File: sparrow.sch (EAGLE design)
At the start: 40 parts, among them Y1 12MHz

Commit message: Further work
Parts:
- added ADC: HEADER-1X8ROUND, anykey:HEADER-1X8ROUND
- added C22, C23: 18p, anykey:CAP_CERAMIC0603
- added C24, C25, C26, C30, C31, C32, C33: 100n, anykey:CAP_CERAMIC0603
- added C27: 1µ, anykey:CAP_CERAMIC0603
- added C28: 470p, anykey:CAP_CERAMIC0603
- added C29: 10µ, anykey:CAP_CERAMIC0603
- added FERRITE_BEAD: BLM18PG121SN1D, anykey:INDUCTOR0603
- added IC1: LAN8720AQFN, anykey:LAN8720AQFN
- added LED2, LED3: (no value), anykey:LED0603
- added P2: ETHERNET_JACKPULSEJACK, anykey:ETHERNET_JACKPULSEJACK
- added R10, R11, R12, R13: 12K, anykey:R-EU_0603
- added R14, R15: 330, anykey:R-EU_0603
- added R16: 12K1, anykey:R-EU_0603
- added R17, R18, R19, R20: 49R9, anykey:R-EU_0603
- added X1: ABS07-32768, anykey:CRYSTAL1206
- added Y2: (no value), anykey:CRYSTAL_WITH_GROUND25X20
- P1: value HEADER-2X5SMD-1.27MM -> DEBUG
- renumbered U$18 to P1
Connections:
- new net ADC0: ADC.1, MCU.ADC0_0
- new net ADC1: ADC.2, MCU.ADC0_1
- new net ADC2: ADC.3, MCU.ADC0_2
- new net ADC3: ADC.4, MCU.ADC0_3
- new net ADC4: ADC.5, MCU.ADC0_4
- new net ADC5: ADC.6, MCU.ADC0_5
- new net ADC6: ADC.7, MCU.ADC0_6
- new net ADC7: ADC.8, MCU.ADC0_7
- new net ETH_!RST: IC1.!RST
- new net ETH_CRS_DV: IC1.CRS_DV/MODE2, MCU.P1_16
- new net ETH_MDC: IC1.MDC, MCU.P7_7
- new net ETH_MDIO: IC1.MDIO, MCU.P1_17
- new net ETH_RBIAS: IC1.RBIAS, R16.2
- new net ETH_REFCLK: IC1.!INT!/REFCLK0
- new net ETH_RTERM: C33.P$1, R19.2, R20.1
- new net ETH_RXD0: IC1.RXD0/MODE0, MCU.P1_15
- new net ETH_RXD1: IC1.RXD1/MODE1, MCU.P0_0
- new net ETH_RXER: IC1.RXER/PHYAD0
- new net ETH_RXN: IC1.RXN, P2.RD-, R20.2
- new net ETH_RXP: IC1.RXP, P2.RD+, R19.1
- new net ETH_TTERM: C32.P$1, R17.2, R18.1
- new net ETH_TXD0: IC1.TXD0, MCU.P1_18
- new net ETH_TXD1: IC1.TXD1, MCU.P1_20
- new net ETH_TXEN: IC1.TXEN, MCU.P0_1
- new net ETH_TXN: IC1.TXN, P2.TD-, R18.2
- new net ETH_TXP: IC1.TXP, P2.TD+, R17.1
- new net ETH_VDDCR: C27.P$1, C28.P$1, IC1.VDDCR
- new net ETH_XTAL1: IC1.XTAL1/CLKIN, Y2.2
- new net ETH_XTAL2: IC1.XTAL2, Y2.1
- new net N$10: IC1.LED2/!INTSEL, LED3.ANODE
- new net N$11: IC1.LED1/REGOFF, LED2.ANODE
- new net N$3: C22.P$1, MCU.RTCX1, X1.2
- new net N$4: C23.P$1, MCU.RTCX2, X1.1
- new net N$6: LED2.CATHODE, R14.2
- new net N$7: LED3.CATHODE, R15.2
- new net SWDCLK: MCU.TCK_SWDCLK, P1.4, R13.2
- new net SWDIO: MCU.TMS_SWDIO, P1.2, R10.1
- new net TDI: MCU.TDI, P1.8, R12.1
- new net TDO_SWO: MCU.TDO_SWO, P1.6, R11.1
- new net VETH33: C24.P$1, C25.P$1, C30.P$1, C31.P$1, FERRITE_BEAD.2, IC1.VDD1A, IC1.VDD2A, P2.RC, P2.TC
- net !RESET: now also P1.10
- net GND: now also C22.P$2, C23.P$2, C24.P$2, C25.P$2, C26.P$2, C27.P$2, C28.P$2, C29.P$2, C30.P$2, C31.P$2, C32.P$2, C33.P$2, IC1.VSS, P1.3, P1.5, P1.9, P2.GND, R13.1, R14.1, R15.1, R16.1, Y2.GND
- net VD33: now also C26.P$1, C29.P$1, FERRITE_BEAD.1, IC1.VDDIO, P1.1, R10.2, R11.2, R12.2

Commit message: Further work
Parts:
- removed C30: 100n, anykey:CAP_CERAMIC0603
- removed FERRITE_BEAD: BLM18PG121SN1D, anykey:INDUCTOR0603
- removed LED2, LED3: (no value), anykey:LED0603
- removed P2: ETHERNET_JACKPULSEJACK, anykey:ETHERNET_JACKPULSEJACK
- added ANT1, ANT2: (no value), anykey:ANTENNA_MONOPOLE1206
- added C34, C52, C53, C54: (no value), anykey:CAP_CERAMIC0603
- added C35, C36, C37, C56: 1µ, anykey:CAP_CERAMIC0603
- added C38, C39, C43, C45, C47, C49: 0.1µ, anykey:CAP_CERAMIC0603
- added C40, C41: 22µ, anykey:CAP_CERAMIC0603
- added C42, C44, C46, C48: 10µ, anykey:CAP_CERAMIC0603
- added C50, C51: 47µ, anykey:CAP_CERAMIC0805
- added C55: (no value), anykey:CAP_CERAMIC0402
- added C57, C59: 22µ 10V, anykey:CAP_CERAMIC0805
- added C58: 100n, anykey:CAP_CERAMIC0603
- added C60: 150µ 10V, anykey:CPOL-EU1210
- added C61: 47n, anykey:CAP_CERAMIC0402
- added C62, C63, C64: 100n, anykey:CAP_CERAMIC0402
- added C65: 1n, anykey:CAP_CERAMIC0402
- added C66, C67: 12p, anykey:CAP_CERAMIC0402
- added C68, C69: 9p, anykey:CAP_CERAMIC0402
- added C70, C72: 2.2p, anykey:CAP_CERAMIC0402
- added C71, C73: 1p, anykey:CAP_CERAMIC0402
- added D1, D2, D3, D4, D5: (no value), anykey:DIODESOD123FL
- added HEADPHONE, LINEIN: (no value), anykey:HEADER-1X3ROUND
- added IC2: TLV320AIC3100VIAS, anykey:TLV320AIC3100VIAS
- added IC3: TPS2500, anykey:TPS2500SON10
- added JP1, U$44, U$45, U$50, U$51, U$52, U$53, U$54, U$55, U$56, U$61, U$62: JUMPERSOLDER_CLOSED, anykey:JUMPERSOLDER_CLOSED
- added L10: 3.3nH, anykey:INDUCTOR0402
- added L2, L3, L4: BLM18PG121SN1D, anykey:INDUCTOR0603
- added L5, L6: (no value), anykey:INDUCTOR0402
- added L7: 2.2µ, anykey:INDUCTOR40X40MM
- added L8: 4.7nH, anykey:INDUCTOR0402
- added L9: 10nH, anykey:INDUCTOR0402
- added MCU1: NRF51822QFN48, anykey:NRF51822QFN48
- added MIC, SPEAKER: (no value), anykey:HEADER-1X2ROUND
- added P3: HEADER-1X9ROUND, anykey:HEADER-1X9ROUND
- added P4: SD_CARD, anykey:SD_CARD
- added P5, P6: (no value), anykey:HEADER-1X5ROUND
- added R21, R29, R34: (no value), anykey:R-EU_0603
- added R22, R23: 2K2, anykey:R-EU_0603
- added R24, R25, R27, R28, R31, R33, R35, R36: 100K, anykey:R-EU_0603
- added R26: 40K2, anykey:R-EU_0603
- added R30, R32: 10K, anykey:R-EU_0603
- added T1, T2, T3: (no value), anykey:PMOS_ENH
- added U$6: ETHERNET_JACK_LEDSRB1-125BAG1A, anykey:ETHERNET_JACK_LEDSRB1-125BAG1A
- added U$68: HEADER-2X5SMD-1.27MM, anykey:HEADER-2X5SMD-1.27MM
- added WIFI1: CC3000EXTENDED, anykey:CC3000EXTENDED
- added X2: 50MHZ, anykey:OSCILLATOR25X20
- added X3: 32.768KHz, anykey:CRYSTAL1206
- L1: value 10u -> 10µH
- Y2: value (none) -> 16MHz
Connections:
- net ETH_RXER renamed ETH_RX_ER
- removed net ETH_REFCLK: IC1.!INT!/REFCLK0
- removed net ETH_XTAL1: IC1.XTAL1/CLKIN, Y2.2
- removed net ETH_XTAL2: IC1.XTAL2, Y2.1
- removed net N$10: IC1.LED2/!INTSEL, LED3.ANODE
- removed net VEXT: MCU.USB0_VBUS, USB0.VBUS
- removed net VUSB: C9.P$1, PWR1.EN_BUCK, PWR1.VCC, R4.2
- new net !AUDIO_PWR: T3.G
- new net !ETH_PWR: T1.G
- new net !WIFI_PWR: T2.G
- new net 5V_BOOST_SW: IC3.SW, L7.2
- new net 5V_GEN_EN: IC3.EN, R29.2
- new net 5V_ILIM: IC3.ILIM, R26.2
- new net AUDIO_!RESET: IC2.!RESET
- new net AUDIO_BCLK: IC2.BCLK, U$54.P$2, U$55.P$2
- new net AUDIO_DIN: IC2.DIN, U$50.P$2
- new net AUDIO_DOUT: IC2.DOUT, U$51.P$2
- new net AUDIO_GPIO1: IC2.GPIO1
- new net AUDIO_MCLK: IC2.MCLK, U$56.P$2
- new net AUDIO_SCL: IC2.SCL, U$62.P$2
- new net AUDIO_SDA: IC2.SDA, U$61.P$2
- new net AUDIO_WCLK: IC2.WCLK, U$52.P$2, U$53.P$2
- new net ETH_LED1: IC1.LED1/REGOFF, R14.2
- new net ETH_LED2: IC1.LED2/!INTSEL, R15.2
- new net ETH_REF_CLK: IC1.XTAL1/CLKIN, MCU.CLK0, X2.CLK
- new net HPL: C50.P$1, IC2.HPL
- new net HPR: C51.P$1, IC2.HPR
- new net HP_L: C50.P$2, HEADPHONE.1
- new net HP_R: C51.P$2, HEADPHONE.3
- new net I2C0_IRQA: P5.4
- new net I2C0_IRQB: P6.4
- new net I2C0_SCL: MCU.I2C0_SCL, P5.2, P6.2, R22.1, U$62.P$1
- new net I2C0_SDA: MCU.I2C0_SDA, P5.3, P6.3, R23.1, U$61.P$1
- new net I2S_MCLK: MCU.P1_19, P3.3, U$56.P$1
- new net I2S_RX_SCK: MCU.P6_0, P3.4, U$55.P$1
- new net I2S_RX_SD: MCU.P6_2, P3.8, U$51.P$1
- new net I2S_RX_WS: MCU.P6_1, P3.6, U$53.P$1
- new net I2S_TX_SCK: MCU.P4_7, P3.5, U$54.P$1
- new net I2S_TX_SD: MCU.P7_2, P3.9, U$50.P$1
- new net I2S_TX_WS: MCU.P7_1, P3.7, U$52.P$1
- new net JP1: JP1.P$2, WIFI1.SCL_EEPROM
- new net LINEIN1: C52.P$1, LINEIN.3
- new net LINEIN2: C53.P$1, LINEIN.1
- new net MIC: C54.P$1, IC2.VOL/MICDET, MIC.2, R21.1
- new net MIC1LM: C52.P$2, IC2.MIC1LM
- new net MIC1LP: C53.P$2, IC2.MIC1LP
- new net MIC1RP: C54.P$2, IC2.MIC1RP
- new net MICBIAS: IC2.MICBIAS, R21.2
- new net N$12: U$45.P$1, WIFI1.SDA_CC3000
- new net N$13: C67.P$1, MCU1.XC2, Y2.1
- new net N$14: C66.P$1, MCU1.XC1, Y2.2
- new net N$15: C62.P$1, MCU1.DEC1
- new net N$16: C61.P$1, MCU1.DEC2
- new net N$17: C69.P$2, MCU1.P0.27, X3.1
- new net N$18: C68.P$2, MCU1.P0.26, X3.2
- new net N$19: R14.1, U$6.LED1A
- new net N$20: D5.ANODE, U$44.P$2
- new net N$21: L8.1, L9.2, MCU1.ANT1
- new net N$22: R15.1, U$6.LED2K
- new net N$23: C70.P$1, L8.2, MCU1.ANT2
- new net N$24: C70.P$2, C71.P$2, L10.1
- new net N$25: ANT2.ANT, C73.P$2, L10.2
- new net N$27: C72.P$2, L9.1, MCU1.VDD_PA
- new net N$5: C55.P$1, L5.2, WIFI1.RF_ANT
- new net NRF_SWDCLK: MCU1.SWDCLK, R34.2, U$68.4
- new net NRF_SWDIO: MCU1.SWDIO/NRESET, U$68.2
- new net SD_CD: MCU.P1_13, P4.CD, R24.1
- new net SD_CLK: MCU.CLK2, P4.5
- new net SD_CMD: MCU.P1_6, P4.2
- new net SD_DAT0: MCU.P1_9, P4.7
- new net SD_DAT1: MCU.P1_10, P4.8
- new net SD_DAT2: MCU.P1_11, P4.9
- new net SD_DAT3: MCU.P1_12, P4.1
- new net SD_WP: P4.WP, R25.1
- new net SPKM: IC2.SPKM, SPEAKER.2
- new net SPKP: IC2.SPKP, SPEAKER.1
- new net USB0_VBUS: MCU.USB0_VBUS, R30.1, R31.2
- new net USB1_VBUS: MCU.P2_5, R32.1, R33.2
- new net USB_PPWR: IC3.ENUSB, MCU.P2_0, R28.2
- new net USB_PWR_FAULT: IC3.!FAULT, MCU.P2_1, R27.1
- new net V5_GEN: C59.P$1, D3.ANODE, IC3.AUX
- new net V5_IN: C9.P$1, D1.CATHODE, D2.CATHODE, PWR1.EN_BUCK, PWR1.VCC, R35.2, R4.2
- new net V5_IN_SENSE: R35.1, R36.2
- new net V5_OUT: D3.CATHODE, D4.CATHODE, D5.CATHODE
- new net VAUDIO33: C37.P$1, C42.P$1, C43.P$1, C44.P$1, C45.P$1, C46.P$1, C47.P$1, C48.P$1, C49.P$1, IC2.AVDD, IC2.DVDD, IC2.HPVDD, IC2.IOVDD, L4.2
- new net VAUDIO5: C38.P$1, C39.P$1, C40.P$1, C41.P$1, IC2.SPKVDD
- new net VETH_RAW: L2.1, T1.D
- new net VETH_RAW1: L3.1, T2.D
- new net VETH_RAW2: L4.1, T3.D
- new net VPOWER: D1.ANODE, D4.ANODE
- new net VUSB0: C60.+, IC3.USB, R30.2, USB0.VBUS
- new net VUSB1: D2.ANODE, R32.2, U$44.P$1, USB1.VBUS
- new net VWIFI33: C36.P$1, L3.2, WIFI1.VBAT_IN, WIFI1.VIO_HOST
- new net WIFI_CLK: WIFI1.SPI_CLK
- new net WIFI_IRQ: WIFI1.SPI_IRQ
- new net WIFI_MISO: WIFI1.SPI_DOUT
- new net WIFI_MOSI: WIFI1.SPI_DIN
- new net WIFI_SSEL: WIFI1.SPI_CS
- new net WIFI_SW_EN: WIFI1.VBAT_SW_EN
- net ETH_RXN: now also U$6.RD-; no longer P2.RD-
- net ETH_RXP: now also U$6.RD+; no longer P2.RD+
- net ETH_TXN: now also U$6.TD-; no longer P2.TD-
- net ETH_TXP: now also U$6.TD+; no longer P2.TD+
- net GND: now also C34.P$2, C35.P$2, C36.P$2, C37.P$2, C38.P$2, C39.P$2, C40.P$2, C41.P$2, C42.P$2, C43.P$2, C44.P$2, C45.P$2, C46.P$2, C47.P$2, C48.P$2, C49.P$2, C56.P$2, C57.P$2, C58.P$2, C59.P$2, C60.-, C61.P$2, C62.P$2, C63.P$2, C64.P$2, C65.P$2, C66.P$2, C67.P$2, C68.P$1, C69.P$1, C71.P$1, C72.P$1, C73.P$1, HEADPHONE.2, IC2.AVSS, IC2.DVSS, IC2.HPVSS, IC2.IOVSS, IC2.SPKVSS, IC3.GND, IC3.PGND, L5.1, L6.1, LINEIN.2, MIC.1, P3.1, P4.3, P4.6, P4.GND, P5.5, P6.5, R26.1, R28.1, R29.1, R31.1, R33.1, R34.1, R36.1, U$6.GND, U$6.LED1K, U$68.3, U$68.5, U$68.7, U$68.9, WIFI1.GND, X2.GND; no longer C30.P$2, P2.GND, R14.1, R15.1
- net N$11: now also JP1.P$1, WIFI1.SCL_CC3000; no longer IC1.LED1/REGOFF, LED2.ANODE
- net N$6: now also ANT1.ANT, C55.P$2, L6.2; no longer LED2.CATHODE, R14.2
- net N$7: now also U$45.P$2, WIFI1.SDA_EEPROM; no longer LED3.CATHODE, R15.2
- net VBAT: now also C57.P$1, C58.P$1, IC3.IN, L7.1
- net VD33: now also C56.P$1, C63.P$1, C64.P$1, C65.P$1, MCU1.AVDD, MCU1.VDD, P3.2, P4.4, P5.1, P6.1, R22.2, R23.2, R24.2, R25.2, R27.2, T1.S, T2.S, T3.S, U$68.1; no longer C26.P$1, C29.P$1, FERRITE_BEAD.1, IC1.VDDIO
- net VETH33: now also C26.P$1, C29.P$1, C34.P$1, C35.P$1, IC1.VDDIO, L2.2, U$6.LED2A, U$6.TC, X2.EN, X2.VDD; no longer C30.P$1, FERRITE_BEAD.2, P2.RC, P2.TC
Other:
- note added: "3.3V supply / battery charger"
- note added: "5V boost / USB OTG supply"
- note added: "5V power distribution"
- note added: "Power domain switches"

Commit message: Further work
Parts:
- removed L2, L3, L4: BLM18PG121SN1D, anykey:INDUCTOR0603
- removed P6: (no value), anykey:HEADER-1X5ROUND
- removed T1, T2, T3: (no value), anykey:PMOS_ENH
- added !PGM: PUSHBUTTONKMR2XX, anykey:PUSHBUTTONKMR2XX
- added C30, C74, C75: 0.1µ, anykey:CAP_CERAMIC0603
- added C76, C77, C78, C79, C80: 1µ, anykey:CAP_CERAMIC0603
- added I2C0, I2C1, P2: (no value), anykey:HEADER-1X5ROUND
- added IC4, IC5, IC6, IC7, IC8: SKYWORKS_AAT4280ASC70JW-8-NOTHERMALS, anykey:SKYWORKS_AAT4280ASC70JW-8-NOTHERMALS
- added IC9: FXMA10820-DFN, anykey:FXMA10820-DFN
- added J1: (no value), anykey:JACK-PLUGCUI_PJ102BH
- added JP2, JP3, SPI0: HEADER-1X7ROUND, anykey:HEADER-1X7ROUND
- added R37: 100K, anykey:R-EU_0603
- added R38, R39: 2K2, anykey:R-EU_0603
- added U$19: JUMPERSOLDER_CLOSED, anykey:JUMPERSOLDER_CLOSED
- added U$26: HEADER-2X5SMD-1.27MM, anykey:HEADER-2X5SMD-1.27MM
- C24, C25, C26, C31, C32, C33, C58, C62, C63, C64: value 100n -> 0.1µ
- C34: value (none) -> 0.1µ
- C35, C36, C37: value 1µ -> 0.1µ
- C61: value 47n -> 0.047µ
- C65: value 1n -> 1000p
- IC1: value LAN8720AQFN -> LAN8720AVIAS; device anykey:LAN8720AQFN -> anykey:LAN8720AVIAS
- P3: value HEADER-1X9ROUND -> HEADER-1X10ROUND; device anykey:HEADER-1X9ROUND -> anykey:HEADER-1X10ROUND
- P5: device anykey:HEADER-1X5ROUND -> anykey:HEADER-1X6ROUND
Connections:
- net I2S_MCLK renamed I2S_RX_MCLK
- net N$1 renamed USB0_RREF
- net N$13 renamed BT_XC2
- net N$14 renamed BT_XC1
- net N$15 renamed BT_DEC1
- net N$16 renamed BT_DEC2
- net N$17 renamed BT_XL1
- net N$18 renamed BT_XL2
- net N$2 renamed CHARGE_SW
- net N$21 renamed BT_ANT1
- net N$23 renamed BT_ANT2
- net N$24 renamed BT_ANT_UNBAL
- net N$25 renamed BT_ANT
- net N$27 renamed BT_VDD_PA
- net N$3 renamed RTXC1
- net N$4 renamed RTXC2
- net N$5 renamed WIFI_ANT_UNBAL
- net N$6 renamed WIFI_ANT
- net N$8 renamed CHARGE_!CHRG
- net USB_PPWR renamed USB0_PPWR
- net USB_PWR_FAULT renamed USB0_PWR_FAULT
- removed net !AUDIO_PWR: T3.G
- removed net !ETH_PWR: T1.G
- removed net !WIFI_PWR: T2.G
- removed net I2C0_IRQA: P5.4
- removed net I2C0_IRQB: P6.4
- removed net JP1: JP1.P$2, WIFI1.SCL_EEPROM
- removed net N$11: JP1.P$1, WIFI1.SCL_CC3000
- removed net N$12: U$45.P$1, WIFI1.SDA_CC3000
- removed net N$7: U$45.P$2, WIFI1.SDA_EEPROM
- removed net VETH_RAW: L2.1, T1.D
- removed net VETH_RAW1: L3.1, T2.D
- removed net VETH_RAW2: L4.1, T3.D
- removed net WIFI_CLK: WIFI1.SPI_CLK
- removed net WIFI_MISO: WIFI1.SPI_DOUT
- removed net WIFI_MOSI: WIFI1.SPI_DIN
- removed net WIFI_SSEL: WIFI1.SPI_CS
- new net !PGM: !PGM.2, MCU.P2_7, R37.1
- new net AUDIO_PWR: IC6.ON_!OFF, IC7.ON_!OFF
- new net ETH_PWR: IC4.ON_!OFF
- new net GPIO5V_1: IC9.B3, JP2.3
- new net GPIO5V_2: IC9.B4, JP2.4
- new net GPIO5V_3: IC9.B5, JP2.5
- new net GPIO5V_4: IC9.B6, JP2.6
- new net GPIO5V_5: IC9.B7, JP2.7
- new net GPIO_1: IC9.A3
- new net GPIO_2: IC9.A4
- new net GPIO_3: IC9.A5
- new net GPIO_4: IC9.A6
- new net GPIO_5: IC9.A7
- new net I2C0_IRQ: I2C0.5
- new net I2C1_IRQ: I2C1.5
- new net I2C1_SCL: I2C1.3, MCU.P2_4, R39.1
- new net I2C1_SDA: I2C1.4, MCU.P2_3, R38.1
- new net I2S_TX_MCLK: MCU.P3_0, P3.10
- new net PORT_PWR_5V: IC8.ON_!OFF
- new net SPI0_IRQ: SPI0.6
- new net SPI0_MISO: MCU.P3_6, SPI0.2
- new net SPI0_MOSI: MCU.P3_7, SPI0.3
- new net SPI0_SCK: MCU.P3_3, SPI0.5
- new net SPI0_SSEL: MCU.P3_8, SPI0.4
- new net SPI1_MISO: MCU.P1_3, WIFI1.SPI_DOUT
- new net SPI1_MOSI: MCU.P1_4, WIFI1.SPI_DIN
- new net SPI1_SCK: MCU.PF_4, WIFI1.SPI_CLK
- new net SPI1_SSEL: MCU.P1_5, WIFI1.SPI_CS
- new net UART0_RXD: IC9.A1, MCU.P6_5
- new net UART0_RXD_5V: IC9.B1, P2.4
- new net UART0_TXD: IC9.A0, MCU.P6_4
- new net UART0_TXD_5V: IC9.B0, P2.3
- new net UART0_UCLK: IC9.A2, MCU.P2_2
- new net UART0_UCLK_5V: IC9.B2, P2.5
- new net UART1_CTS: MCU.P5_4
- new net UART1_DCD: MCU.P5_5
- new net UART1_DSR: MCU.P5_0
- new net UART1_DTR: MCU.P5_1
- new net UART1_RI: MCU.P5_3
- new net UART1_RTS: MCU.P5_2
- new net UART1_RXD: MCU.P5_7
- new net UART1_TXD: MCU.P5_6
- new net UART2_DIR: MCU.P2_13, P5.6
- new net UART2_RXD: MCU.P2_11, P5.4
- new net UART2_TXD: MCU.P2_10, P5.3
- new net UART2_UCLK: MCU.P2_12, P5.5
- new net UART3_BAUD: JP3.7, MCU.P4_3
- new net UART3_DIR: JP3.6, MCU.P4_4
- new net UART3_RXD: JP3.4, MCU.P4_2
- new net UART3_TXD: JP3.3, MCU.P4_1
- new net UART3_UCLK: JP3.5, MCU.P4_0
- new net VPORT5: C75.P$1, IC8.OUT, IC9.VCCB, JP2.1, P2.1
- new net WIFI_PWR: IC5.ON_!OFF
- new net WIFI_SCL_CC3000: JP1.P$1, U$26.8, WIFI1.SCL_CC3000
- new net WIFI_SCL_EEPROM: JP1.P$2, U$26.9, WIFI1.SCL_EEPROM
- new net WIFI_SDA_CC3000: U$26.6, U$45.P$1, WIFI1.SDA_CC3000
- new net WIFI_SDA_EEPROM: U$26.7, U$45.P$2, WIFI1.SDA_EEPROM
- new net WL_EN1: U$19.P$1, U$26.2, WIFI1.WL_EN1
- new net WL_EN2: U$19.P$2, U$26.3, WIFI1.WL_EN2
- new net WL_RS232_RX: U$26.5, WIFI1.WL_RS232_RX
- new net WL_RS232_TX: U$26.4, WIFI1.WL_RS232_TX
- net GND: now also !PGM.1, C30.P$2, C74.P$2, C75.P$2, C76.P$2, C77.P$2, C78.P$2, C79.P$2, C80.P$2, I2C0.2, I2C1.2, IC4.GND, IC5.GND, IC6.GND, IC7.GND, IC8.GND, IC9.!OE, IC9.GND, J1.1, J1.2, JP2.2, JP3.2, MCU.P1_1, MCU.P2_9, P2.2, P3.2, P5.2, SPI0.7, U$26.10; no longer P3.1, P5.5, P6.5
- net I2C0_SCL: now also I2C0.3; no longer P5.2, P6.2
- net I2C0_SDA: now also I2C0.4; no longer P5.3, P6.3
- net V5_OUT: now also C79.P$1, C80.P$1, IC7.IN, IC8.IN
- net VAUDIO33: now also IC6.OUT; no longer L4.2
- net VAUDIO5: now also C74.P$1, IC7.OUT
- net VD33: now also C76.P$1, C77.P$1, C78.P$1, I2C0.1, I2C1.1, IC4.IN, IC5.IN, IC6.IN, IC9.VCCA, JP3.1, MCU.!TRST, MCU.P1_2, MCU.P2_8, P3.1, R37.2, R38.2, R39.2, SPI0.1; no longer P3.2, P6.1, T1.S, T2.S, T3.S
- net VETH33: now also IC4.OUT; no longer L2.2
- net VPOWER: now also J1.3
- net VWIFI33: now also C30.P$1, IC5.OUT, U$26.1; no longer L3.2
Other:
- note added: "Plugs"
- moved on the sheet: ADC, ANT1, BATT, C1, C2, C21, C22, C23, C35, C36, C37, C55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

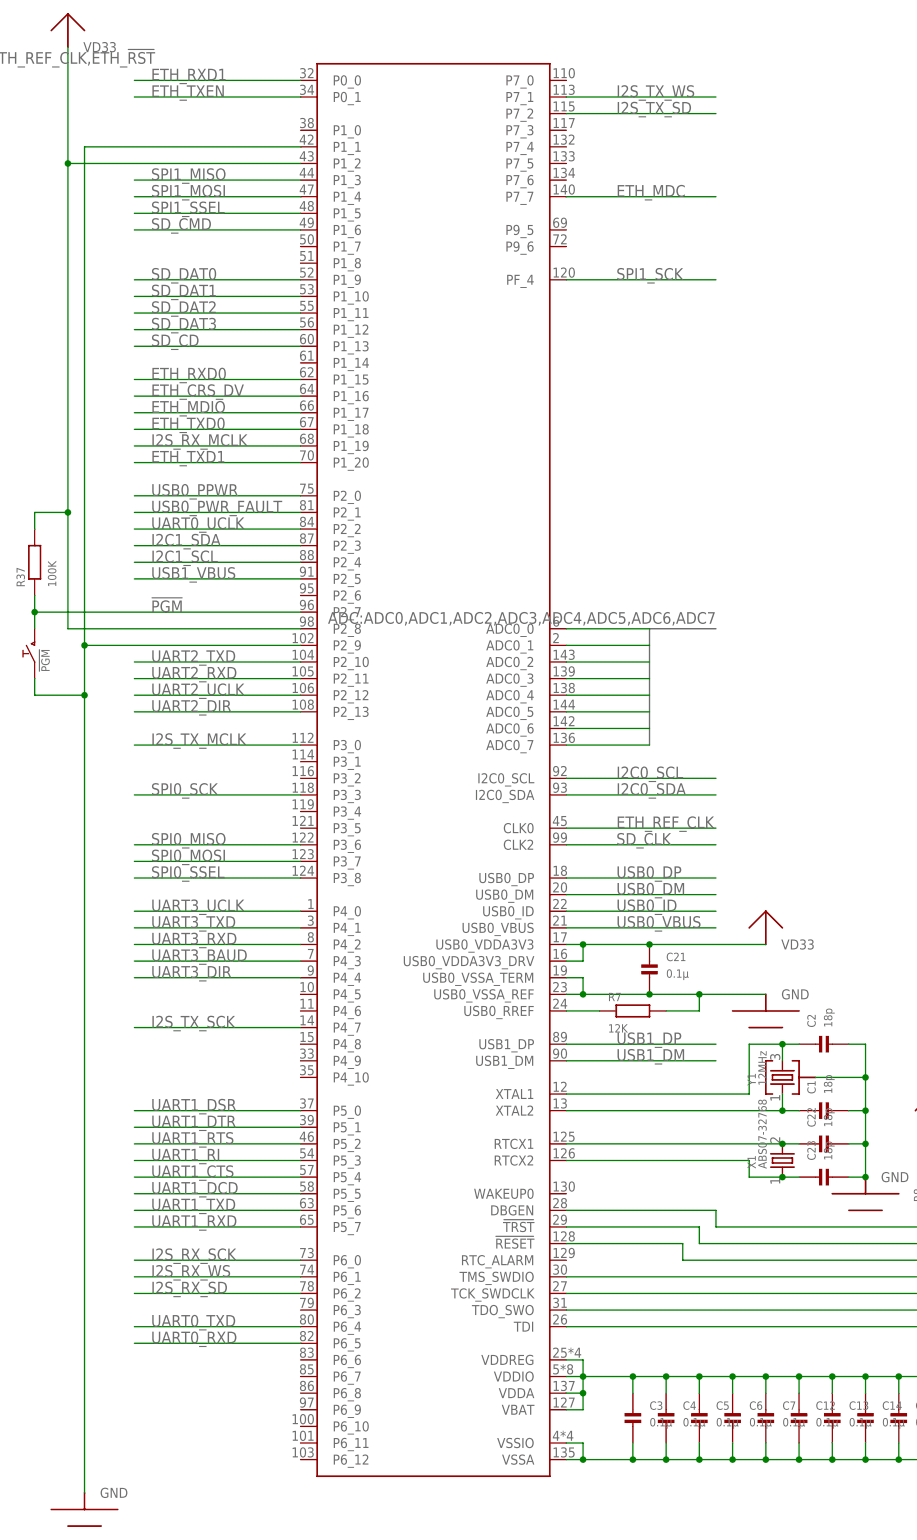
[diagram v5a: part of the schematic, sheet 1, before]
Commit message: basic routing finished
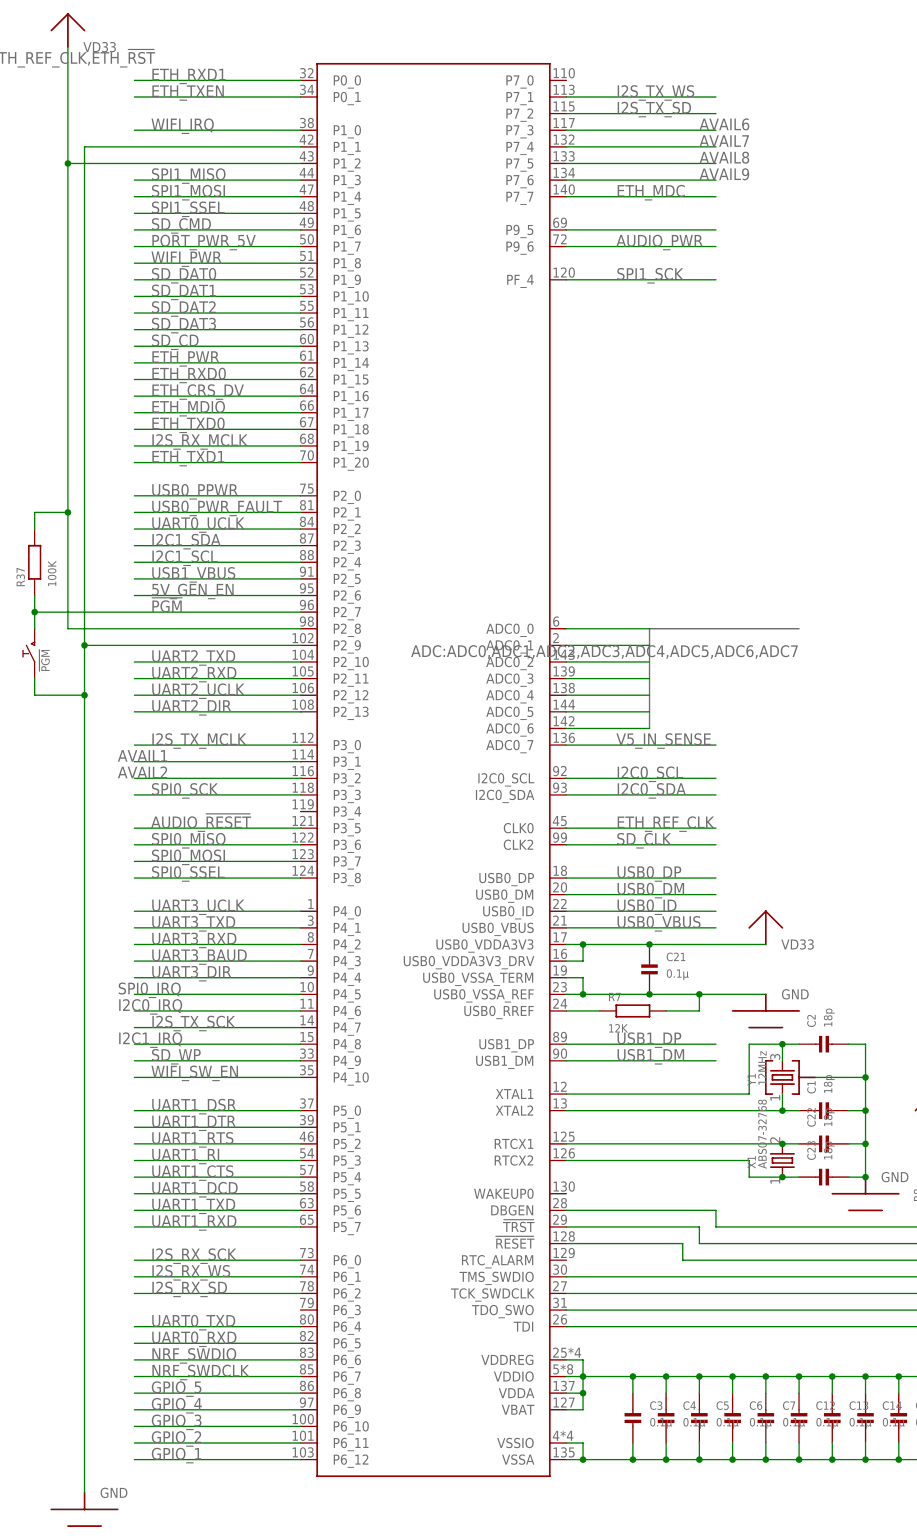
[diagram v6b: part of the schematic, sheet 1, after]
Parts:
- removed ADC: HEADER-1X8ROUND, anykey:HEADER-1X8ROUND
- added JP4: HEADER-1X7ROUND, anykey:HEADER-1X7ROUND
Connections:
- removed net ADC7: ADC.8, MCU.ADC0_7
- new net AVAIL1: MCU.P3_1
- new net AVAIL2: MCU.P3_2
- new net AVAIL6: MCU.P7_3
- new net AVAIL7: MCU.P7_4
- new net AVAIL8: MCU.P7_5
- new net AVAIL9: MCU.P7_6
- net 5V_GEN_EN: now also MCU.P2_6
- net ADC0: now also JP4.1; no longer ADC.1
- net ADC1: now also JP4.2; no longer ADC.2
- net ADC2: now also JP4.3; no longer ADC.3
- net ADC3: now also JP4.4; no longer ADC.4
- net ADC4: now also JP4.5; no longer ADC.5
- net ADC5: now also JP4.6; no longer ADC.6
- net ADC6: now also JP4.7; no longer ADC.7
- net AUDIO_!RESET: now also MCU.P3_5
- net AUDIO_PWR: now also MCU.P9_6
- net ETH_!RST: now also MCU.P9_5
- net ETH_PWR: now also MCU.P1_14
- net GPIO_1: now also MCU.P6_12
- net GPIO_2: now also MCU.P6_11
- net GPIO_3: now also MCU.P6_10
- net GPIO_4: now also MCU.P6_9
- net GPIO_5: now also MCU.P6_8
- net I2C0_IRQ: now also MCU.P4_6
- net I2C1_IRQ: now also MCU.P4_8
- net NRF_SWDCLK: now also MCU.P6_7
- net NRF_SWDIO: now also MCU.P6_6
- net PORT_PWR_5V: now also MCU.P1_7
- net SD_WP: now also MCU.P4_9
- net SPI0_IRQ: now also MCU.P4_5
- net UART1_CTS: now also MCU1.P0.03
- net UART1_RTS: now also MCU1.P0.02
- net UART1_RXD: now also MCU1.P0.01
- net UART1_TXD: now also MCU1.P0.00
- net V5_IN_SENSE: now also MCU.ADC0_7
- net WIFI_IRQ: now also MCU.P1_0
- net WIFI_PWR: now also MCU.P1_8
- net WIFI_SW_EN: now also MCU.P4_10
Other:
- moved on the sheet: IC3

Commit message: Silkscreen fixed
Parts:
- removed Y1: 12MHz, anykey:CRYSTAL_WITH_GROUNDABM8G
- added LOGO2, LOGO3, LOGO4: LOGOKRONE, anykey:LOGOKRONE
- added X4: 50MHZ, anykey:OSCILLATOR25X20
- C1: value 18p -> 1000p; device anykey:CAP_CERAMIC0603 -> anykey:CAP_CERAMIC0402
- C65: value 1000p -> 18p; device anykey:CAP_CERAMIC0402 -> anykey:CAP_CERAMIC0603
- X2: value 50MHZ -> 12MHz; device anykey:OSCILLATOR25X20 -> anykey:CRYSTAL_WITH_GROUNDABM8G
- renumbered HEADPHONE to HP, J1 to 5VDC_IN, JP1 to SCL, JP2 to GPIO_5V, JP3 to UART3, JP4 to ADC, LINEIN to LINE, P1 to LPC_DEBUG, P2 to UART_5V, P3 to I2S, P4 to SD_CARD, P5 to UART2, SPEAKER to LS, U$19 to WL_EN, U$26 to CC_DEBUG, U$44 to LIM, U$45 to SDA, U$50 to TX_SD, U$51 to RX_SD, U$52 to TX_WS, U$53 to RX_WS, U$54 to TX_SCK, U$55 to RX_SCK, U$56 to MCLK, U$61 to A_SDA, U$62 to A_SCL, U$68 to NRF_DEBUG, WIFI1 to WIFI
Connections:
- net ETH_REF_CLK: now also X4.CLK; no longer X2.CLK
- net GND: now also X4.GND; no longer Y1.GND
- net VD33: now also C1.P$1; no longer C65.P$1
- net VETH33: now also X4.EN, X4.VDD; no longer X2.EN, X2.VDD
- net XTAL1: now also X2.2; no longer Y1.2
- net XTAL2: now also C65.P$1, X2.1; no longer C1.P$1, Y1.1
